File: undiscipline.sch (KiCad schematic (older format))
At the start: 166 parts, among them J1 Conn_01x04_Male, J2 USB_B_Micro, SW1 SW_Push, SW10 SW_Push, SW11 SW_Push, SW12 SW_Push, SW13 SW_Push, SW14 SW_Push, SW15 SW_Push, SW16 SW_Push, SW17 SW_Push, SW18 SW_Push, SW19 SW_Push, SW2 SW_Push, SW20 SW_Push, SW21 SW_Push, SW22 SW_Push, SW23 SW_Push, SW24 SW_Push, SW25 SW_Push, SW26 SW_Push, SW27 SW_Push, SW28 SW_Push, SW29 SW_Push, SW3 SW_Push, SW30 SW_Push, SW31 SW_Push, SW32 SW_Push, SW33 SW_Push, SW34 SW_Push, SW35 SW_Push, SW36 SW_Push, SW37 SW_Push, SW38 SW_Push, SW39 SW_Push, SW4 SW_Push, SW40 SW_Push, SW41 SW_Push, SW42 SW_Push, SW43 SW_Push, SW44 SW_Push, SW45 SW_Push, SW46 SW_Push, SW47 SW_Push, SW48 SW_Push, SW49 SW_Push, SW5 SW_Push, SW50 SW_Push, SW51 SW_Push, SW52 SW_Push, SW53 SW_Push, SW54 SW_Push, SW55 SW_Push, SW56 SW_Push, SW57 SW_Push, SW58 SW_Push, SW59 SW_Push, SW6 SW_Push, SW60 SW_Push, SW61 SW_Push, SW62 SW_Push, SW63 SW_Push, SW64 SW_Push, SW65 SW_Push, SW66 SW_Push, SW67 SW_Push, SW68 SW_Push, SW69 SW_Push, SW7 SW_Push, SW70 SW_Push, SW71 SW_Push, SW72 SW_Push, SW73 SW_Push, SW74 SW_Push, SW75 SW_Push, SW8 SW_Push, SW9 SW_Push, U1 ATmega32A-PU, Y1 16MHz

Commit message: Add LED lights
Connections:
- net LED: now reaches U1.19 (PD5)
- no-connect marks 7 -> 6
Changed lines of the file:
@@
 $Descr A4 11693 8268
 encoding utf-8
-Sheet 1 1
+Sheet 1 2
 Title ""
 Date ""
@@
 Connection ~ 5500 1450
 NoConn ~ 2400 1600
-NoConn ~ 2400 4200
 NoConn ~ 2400 4300
 NoConn ~ 2400 4400
@@
 	0    1    1    0
 $EndComp
+$Sheet
+S 8850 4700 1550 650
+U 5FDEEC30
+F0 "leds" 50
+F1 "leds.sch" 50
+$EndSheet
+Text GLabel 2400 4200 2    50   Input ~ 0
+LED
 $EndSCHEMATC

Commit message: Add LEDs under each key
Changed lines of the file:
@@
 $EndComp
 $Sheet
-S 8850 4700 1550 650
+S 8350 4750 550  650
 U 5FDEEC30
 F0 "leds" 50
 F1 "leds.sch" 50
+F2 "LED" I R 8900 4900 50
 $EndSheet
 Text GLabel 2400 4200 2    50   Input ~ 0
 LED
+Text GLabel 8900 4900 2    50   Input ~ 0
+LED
 $EndSCHEMATC

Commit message: WIP
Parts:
- J1: footprint Connector_PinHeader_1.00mm:PinHeader_1x04_P1.00mm_Vertical -> Connector_PinHeader_2.54mm:PinHeader_1x04_P2.54mm_Vertical
- Y1: footprint Crystal:Crystal_HC18-U_Vertical -> Crystal:Crystal_HC49-4H_Vertical
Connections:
- net +5V: now also J1.2 (Pin_2); no longer J1.4 (Pin_4)
- net GND: now also J1.1 (Pin_1); no longer J1.3 (Pin_3)
- net SCL: now also J1.3 (Pin_3); no longer J1.2 (Pin_2)
- net SDA: now also J1.4 (Pin_4); no longer J1.1 (Pin_1)
- net col0: now also SW53.2
- net col1: no longer SW53.2
- net col10: now also SW71.2
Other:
- moved on the sheet: D53, SW53
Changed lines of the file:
@@
 L Switch:SW_Push SW53
 U 1 1 5FD84B0E
-P 3800 3250
-F 0 "SW53" H 3800 3535 50  0000 C CNN
-F 1 "SW_Push" H 3800 3444 50  0000 C CNN
-F 2 "undiscipline:CherryMX_Kailh_Socket" H 3800 3450 50  0001 C CNN
-F 3 "~" H 3800 3450 50  0001 C CNN
-	1    3800 3250
+P 3300 3250
+F 0 "SW53" H 3300 3535 50  0000 C CNN
+F 1 "SW_Push" H 3300 3444 50  0000 C CNN
+F 2 "undiscipline:CherryMX_Kailh_Socket" H 3300 3450 50  0001 C CNN
+F 3 "~" H 3300 3450 50  0001 C CNN
+	1    3300 3250
 	1    0    0    -1
 $EndComp
@@
 L Device:D D53
 U 1 1 5FD84B14
-P 3600 3400
-F 0 "D53" V 3646 3320 50  0000 R CNN
-F 1 "D" V 3555 3320 50  0000 R CNN
-F 2 "Diode_THT:D_T-1_P5.08mm_Horizontal" H 3600 3400 50  0001 C CNN
-F 3 "~" H 3600 3400 50  0001 C CNN
-	1    3600 3400
+P 3100 3400
+F 0 "D53" V 3146 3320 50  0000 R CNN
+F 1 "D" V 3055 3320 50  0000 R CNN
+F 2 "Diode_THT:D_T-1_P5.08mm_Horizontal" H 3100 3400 50  0001 C CNN
+F 3 "~" H 3100 3400 50  0001 C CNN
+	1    3100 3400
 	0    -1   -1   0
 $EndComp
@@
 Wire Wire Line
 	10100 3550 9600 3550
-Connection ~ 3600 3550
-Wire Wire Line
-	3600 3550 3100 3550
 Connection ~ 4100 3550
-Wire Wire Line
-	4100 3550 3600 3550
 Connection ~ 4600 3550
 Wire Wire Line
@@
 Wire Wire Line
 	3500 2050 3500 2650
-Wire Wire Line
-	4000 2650 4000 3250
-Connection ~ 4000 3250
-Wire Wire Line
-	4000 3250 4000 3850
 Text GLabel 3500 850  1    50   Input ~ 0
 col0
@@
 F 0 "Y1" V 804 1388 50  0000 L CNN
 F 1 "16MHz" V 895 1388 50  0000 L CNN
-F 2 "Crystal:Crystal_HC18-U_Vertical" H 850 1300 50  0001 C CNN
+F 2 "Crystal:Crystal_HC49-4H_Vertical" H 850 1300 50  0001 C CNN
 F 3 "~" H 850 1300 50  0001 C CNN
 	1    850  1300
@@
 Connection ~ 7000 3250
 Wire Wire Line
-	3500 3850 3500 2650
+	3500 3850 3500 3250
 Connection ~ 3500 2650
 Wire Wire Line
@@
 F 0 "J1" H 6608 6131 50  0000 C CNN
 F 1 "Conn_01x04_Male" H 6608 6040 50  0000 C CNN
-F 2 "Connector_PinHeader_1.00mm:PinHeader_1x04_P1.00mm_Vertical" H 6500 5850 50  0001 C CNN
+F 2 "Connector_PinHeader_2.54mm:PinHeader_1x04_P2.54mm_Vertical" H 6500 5850 50  0001 C CNN
 F 3 "~" H 6500 5850 50  0001 C CNN
 	1    6500 5850
 	1    0    0    -1
 $EndComp
-Text GLabel 6700 5750 2    50   Input ~ 0
+Text GLabel 6700 6050 2    50   Input ~ 0
 SDA
-Text GLabel 6700 5850 2    50   Input ~ 0
+Text GLabel 6700 5950 2    50   Input ~ 0
 SCL
 $Comp
 L power:GND #PWR08
 U 1 1 5FDA403D
-P 6700 5950
-F 0 "#PWR08" H 6700 5700 50  0001 C CNN
-F 1 "GND" V 6705 5822 50  0000 R CNN
-F 2 "" H 6700 5950 50  0001 C CNN
-F 3 "" H 6700 5950 50  0001 C CNN
-	1    6700 5950
+P 6700 5750
+F 0 "#PWR08" H 6700 5500 50  0001 C CNN
+F 1 "GND" V 6705 5622 50  0000 R CNN
+F 2 "" H 6700 5750 50  0001 C CNN
+F 3 "" H 6700 5750 50  0001 C CNN
+	1    6700 5750
 	0    -1   -1   0
 $EndComp
@@
 L power:+5V #PWR010
 U 1 1 5FDA4D08
-P 6700 6050
-F 0 "#PWR010" H 6700 5900 50  0001 C CNN
-F 1 "+5V" V 6715 6178 50  0000 L CNN
-F 2 "" H 6700 6050 50  0001 C CNN
-F 3 "" H 6700 6050 50  0001 C CNN
-	1    6700 6050
+P 6700 5850
+F 0 "#PWR010" H 6700 5700 50  0001 C CNN
+F 1 "+5V" V 6715 5978 50  0000 L CNN
+F 2 "" H 6700 5850 50  0001 C CNN
+F 3 "" H 6700 5850 50  0001 C CNN
+	1    6700 5850
 	0    1    1    0
 $EndComp
@@
 Text GLabel 8900 4900 2    50   Input ~ 0
 LED
+Connection ~ 3500 3250
+Wire Wire Line
+	3500 3250 3500 2650
+Wire Wire Line
+	3100 3550 4100 3550
+Wire Wire Line
+	4000 2650 4000 3850
+Wire Wire Line
+	8500 3250 8500 3850
+Connection ~ 8500 3250
 $EndSCHEMATC

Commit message: Add 3d models
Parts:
- J1: footprint Connector_PinHeader_2.54mm:PinHeader_1x04_P2.54mm_Vertical -> undiscipline:OLED128x64
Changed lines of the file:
@@
 F 0 "J1" H 6608 6131 50  0000 C CNN
 F 1 "Conn_01x04_Male" H 6608 6040 50  0000 C CNN
-F 2 "Connector_PinHeader_2.54mm:PinHeader_1x04_P2.54mm_Vertical" H 6500 5850 50  0001 C CNN
+F 2 "undiscipline:OLED128x64" H 6500 5850 50  0001 C CNN
 F 3 "~" H 6500 5850 50  0001 C CNN
 	1    6500 5850

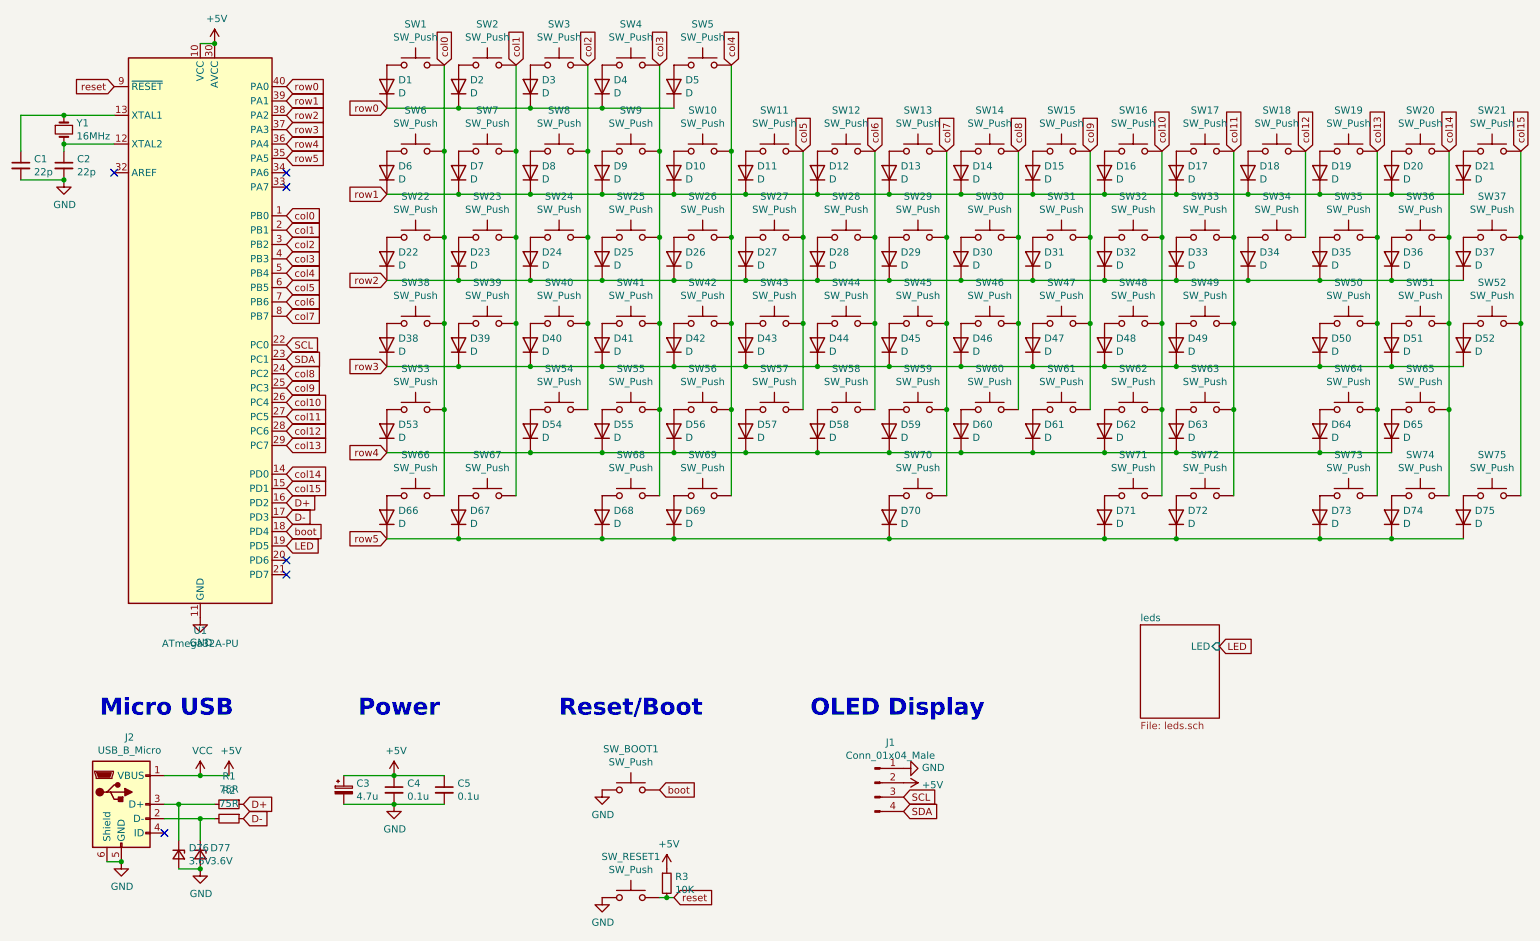
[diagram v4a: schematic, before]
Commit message: Finish routing tracks
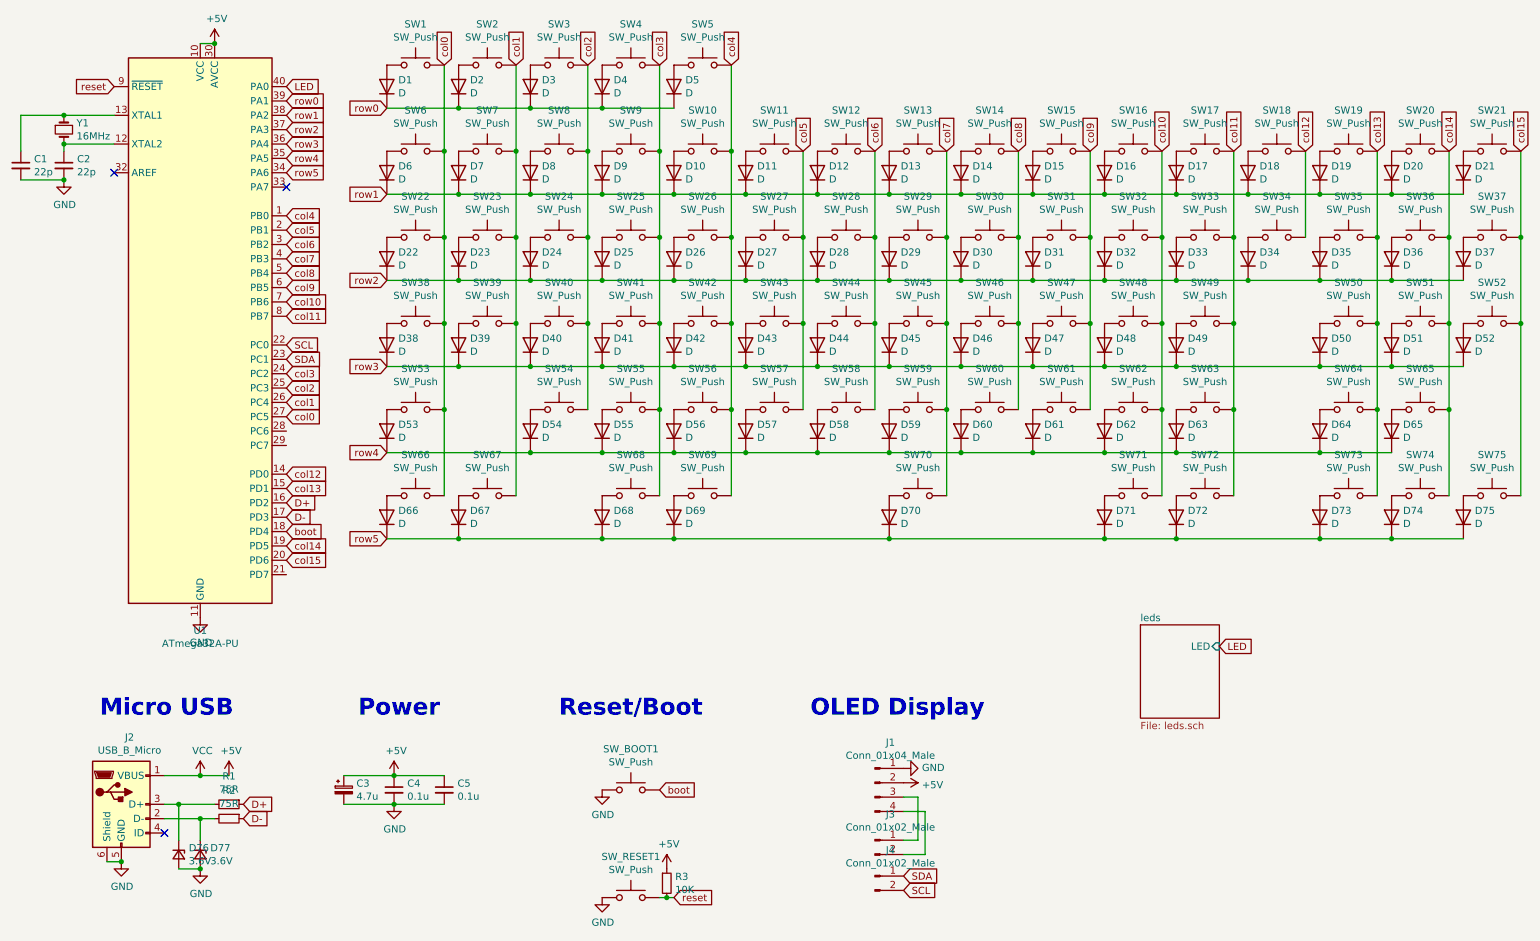
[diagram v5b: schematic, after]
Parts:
- added J3, J4: Conn_01x02_Male, Connector_PinHeader_2.54mm:PinHeader_1x02_P2.54mm_Horizontal, symbol Connector:Conn_01x02_Male
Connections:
- net LED: now also U1.40 (PA0); no longer U1.19 (PD5)
- net SCL: now also J4.2 (Pin_2); no longer J1.3 (Pin_3)
- net SDA: now also J4.1 (Pin_1); no longer J1.4 (Pin_4)
- net col0: now also U1.27 (PC5); no longer U1.1 (PB0)
- net col1: now also U1.26 (PC4); no longer U1.2 (PB1)
- net col10: now also U1.7 (PB6); no longer U1.26 (PC4)
- net col11: now also U1.8 (PB7); no longer U1.27 (PC5)
- net col12: now also U1.14 (PD0); no longer U1.28 (PC6)
- net col13: now also U1.15 (PD1); no longer U1.29 (PC7)
- net col14: now also U1.19 (PD5); no longer U1.14 (PD0)
- net col15: now also U1.20 (PD6); no longer U1.15 (PD1)
- net col2: now also U1.25 (PC3); no longer U1.3 (PB2)
- net col3: now also U1.24 (PC2); no longer U1.4 (PB3)
- net col4: now also U1.1 (PB0); no longer U1.5 (PB4)
- net col5: now also U1.2 (PB1); no longer U1.6 (PB5)
- net col6: now also U1.3 (PB2); no longer U1.7 (PB6)
- net col7: now also U1.4 (PB3); no longer U1.8 (PB7)
- net col8: now also U1.5 (PB4); no longer U1.24 (PC2)
- net col9: now also U1.6 (PB5); no longer U1.25 (PC3)
- net row0: now also U1.39 (PA1); no longer U1.40 (PA0)
- net row1: now also U1.38 (PA2); no longer U1.39 (PA1)
- net row2: now also U1.37 (PA3); no longer U1.38 (PA2)
- net row3: now also U1.36 (PA4); no longer U1.37 (PA3)
- net row4: now also U1.35 (PA5); no longer U1.36 (PA4)
- net row5: now also U1.34 (PA6); no longer U1.35 (PA5)
- new net: J1.3 (Pin_3), J3.1 (Pin_1)
- new net: J1.4 (Pin_4), J3.2 (Pin_2)
- no-connect marks 6 -> 3
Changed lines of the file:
@@
 $EndComp
 Connection ~ 1900 700
-Text GLabel 2400 1300 2    50   Input ~ 0
+Text GLabel 2400 1400 2    50   Input ~ 0
 row3
-Text GLabel 2400 1100 2    50   Input ~ 0
+Text GLabel 2400 1200 2    50   Input ~ 0
 row1
+Text GLabel 2400 3300 2    50   Input ~ 0
+col0
+Text GLabel 2400 3100 2    50   Input ~ 0
+col2
 Text GLabel 2400 1900 2    50   Input ~ 0
-col0
-Text GLabel 2400 2100 2    50   Input ~ 0
-col2
-Text GLabel 2400 2300 2    50   Input ~ 0
 col4
 NoConn ~ 2400 1700
-Text GLabel 2400 1400 2    50   Input ~ 0
+Text GLabel 2400 1500 2    50   Input ~ 0
 row4
-Text GLabel 2400 1200 2    50   Input ~ 0
+Text GLabel 2400 1300 2    50   Input ~ 0
 row2
-Text GLabel 2400 1000 2    50   Input ~ 0
+Text GLabel 2400 1100 2    50   Input ~ 0
 row0
-Text GLabel 2400 2000 2    50   Input ~ 0
+Text GLabel 2400 3200 2    50   Input ~ 0
 col1
+Text GLabel 2400 3000 2    50   Input ~ 0
+col3
+Text GLabel 2400 3800 2    50   Input ~ 0
+col13
+Text GLabel 2400 3700 2    50   Input ~ 0
+col12
+Text GLabel 2400 2600 2    50   Input ~ 0
+col11
+Text GLabel 2400 2500 2    50   Input ~ 0
+col10
+Text GLabel 2400 2400 2    50   Input ~ 0
+col9
+Text GLabel 2400 2300 2    50   Input ~ 0
+col8
 Text GLabel 2400 2200 2    50   Input ~ 0
-col3
-Text GLabel 2400 3500 2    50   Input ~ 0
-col13
-Text GLabel 2400 3400 2    50   Input ~ 0
-col12
-Text GLabel 2400 3300 2    50   Input ~ 0
-col11
-Text GLabel 2400 3200 2    50   Input ~ 0
-col10
-Text GLabel 2400 3100 2    50   Input ~ 0
-col9
-Text GLabel 2400 3000 2    50   Input ~ 0
-col8
-Text GLabel 2400 2600 2    50   Input ~ 0
 col7
 Text GLabel 2400 3900 2    50   Input ~ 0
@@
 Text GLabel 2400 4100 2    50   Input ~ 0
 boot
-Text GLabel 2400 2400 2    50   Input ~ 0
+Text GLabel 2400 2000 2    50   Input ~ 0
 col5
-Text GLabel 2400 2500 2    50   Input ~ 0
+Text GLabel 2400 2100 2    50   Input ~ 0
 col6
-Text GLabel 2400 3700 2    50   Input ~ 0
+Text GLabel 2400 4200 2    50   Input ~ 0
 col14
 $Comp
@@
 	10100 4150 10600 4150
 Connection ~ 10100 4150
-Text GLabel 2400 3800 2    50   Input ~ 0
+Text GLabel 2400 4300 2    50   Input ~ 0
 col15
 Text GLabel 2400 2800 2    50   Input ~ 0
@@
 Text GLabel 2400 2900 2    50   Input ~ 0
 SDA
-Text GLabel 2400 1500 2    50   Input ~ 0
+Text GLabel 2400 1600 2    50   Input ~ 0
 row5
 $Comp
@@
 	5500 850  5500 1450
 Connection ~ 5500 1450
-NoConn ~ 2400 1600
-NoConn ~ 2400 4300
-NoConn ~ 2400 4400
 Text Notes 1100 5400 0    118  ~ 24
 Micro USB
@@
 	1    0    0    -1
 $EndComp
-Text GLabel 6700 6050 2    50   Input ~ 0
-SDA
-Text GLabel 6700 5950 2    50   Input ~ 0
-SCL
 $Comp
 L power:GND #PWR08
@@
 F2 "LED" I R 8900 4900 50
 $EndSheet
-Text GLabel 2400 4200 2    50   Input ~ 0
+Text GLabel 2400 1000 2    50   Input ~ 0
 LED
 Text GLabel 8900 4900 2    50   Input ~ 0
@@
 	8500 3250 8500 3850
 Connection ~ 8500 3250
+$Comp
+L Connector:Conn_01x02_Male J3
+U 1 1 6015AB67
+P 6500 6250
+F 0 "J3" H 6608 6431 50  0000 C CNN
+F 1 "Conn_01x02_Male" H 6608 6340 50  0000 C CNN
+F 2 "Connector_PinHeader_2.54mm:PinHeader_1x02_P2.54mm_Horizontal" H 6500 6250 50  0001 C CNN
+F 3 "~" H 6500 6250 50  0001 C CNN
+	1    6500 6250
+	1    0    0    -1
+$EndComp
+Wire Wire Line
+	6700 5950 6800 5950
+Wire Wire Line
+	6800 5950 6800 6250
+Wire Wire Line
+	6800 6250 6700 6250
+Wire Wire Line
+	6700 6050 6850 6050
+Wire Wire Line
+	6850 6050 6850 6350
+Wire Wire Line
+	6850 6350 6700 6350
+Text GLabel 6700 6600 2    50   Input ~ 0
+SCL
+Text GLabel 6700 6500 2    50   Input ~ 0
+SDA
+$Comp
+L Connector:Conn_01x02_Male J4
+U 1 1 601A0FA2
+P 6500 6500
+F 0 "J4" H 6608 6681 50  0000 C CNN
+F 1 "Conn_01x02_Male" H 6608 6590 50  0000 C CNN
+F 2 "Connector_PinHeader_2.54mm:PinHeader_1x02_P2.54mm_Horizontal" H 6500 6500 50  0001 C CNN
+F 3 "~" H 6500 6500 50  0001 C CNN
+	1    6500 6500
+	1    0    0    -1
+$EndComp
 $EndSCHEMATC
